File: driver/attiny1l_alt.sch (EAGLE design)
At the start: 6 parts, among them IC1 ATTiny85, IC3 74AHC1G00DCK, IC4 LB1973M, J1 AVR_SPI_PRG_6NS

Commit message: correct net name
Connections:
- net N$6 renamed RESET-
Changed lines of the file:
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@@
 </segment>
 </net>
-<net name="N$6" class="0">
+<net name="RESET-" class="0">
 <segment>
 <pinref part="IC1" gate="G$1" pin="PB5/PCINT5/!RESET!/ADC0/DW"/>

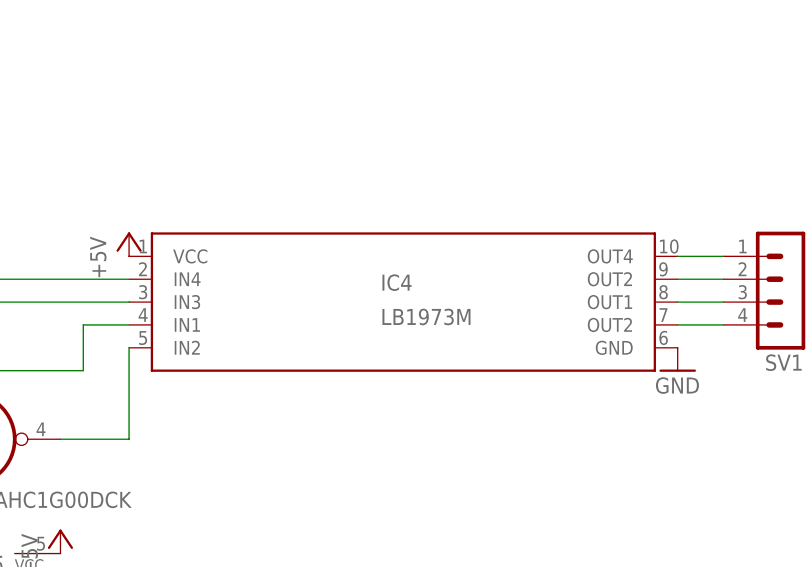
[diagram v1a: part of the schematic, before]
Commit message: the footpring was actually a bit too wide, made it 20mils narrower
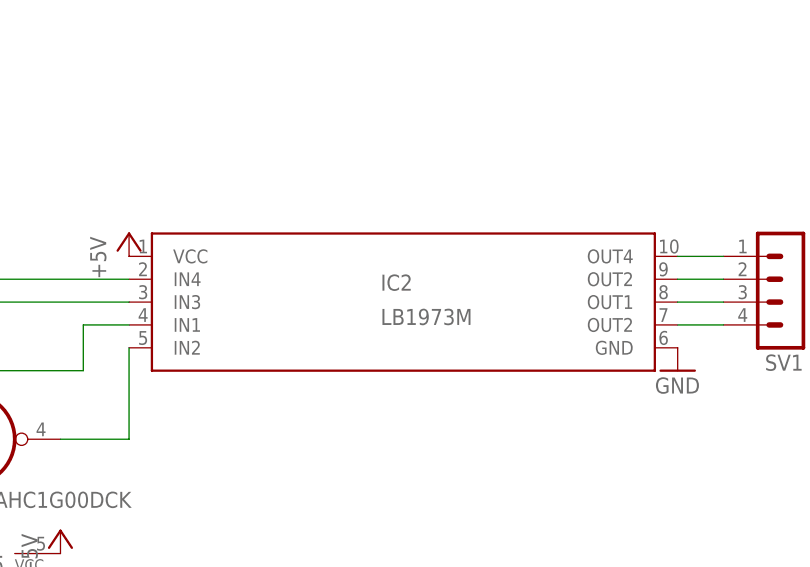
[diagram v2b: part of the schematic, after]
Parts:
- renumbered IC4 to IC2
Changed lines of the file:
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@@
 <part name="P+6" library="supply1" deviceset="+5V" device=""/>
 <part name="GND6" library="supply1" deviceset="GND" device=""/>
-<part name="IC4" library="LB1973M" deviceset="LB1973M" device=""/>
+<part name="IC2" library="LB1973M" deviceset="LB1973M" device=""/>
 </parts>
 <sheets>
@@
 <instance part="P+6" gate="1" x="40.64" y="55.88"/>
 <instance part="GND6" gate="1" x="33.02" y="55.88" rot="R180"/>
-<instance part="IC4" gate="G$1" x="149.86" y="78.74"/>
+<instance part="IC2" gate="G$1" x="149.86" y="78.74"/>
 </instances>
 <busses>
@@
 <wire x1="111.76" y1="63.5" x2="119.38" y2="63.5" width="0.1524" layer="91"/>
 <wire x1="119.38" y1="63.5" x2="119.38" y2="73.66" width="0.1524" layer="91"/>
-<pinref part="IC4" gate="G$1" pin="IN2"/>
+<pinref part="IC2" gate="G$1" pin="IN2"/>
 </segment>
 </net>
 <net name="IN4" class="0">
 <segment>
-<pinref part="IC4" gate="G$1" pin="IN4"/>
 <pinref part="IC1" gate="G$1" pin="PB4/PCINT4/ADC2"/>
 <wire x1="50.8" y1="78.74" x2="96.52" y2="78.74" width="0.1524" layer="91"/>
 <wire x1="96.52" y1="78.74" x2="96.52" y2="81.28" width="0.1524" layer="91"/>
 <wire x1="96.52" y1="81.28" x2="119.38" y2="81.28" width="0.1524" layer="91"/>
+<pinref part="IC2" gate="G$1" pin="IN4"/>
 </segment>
 </net>
@@
 <wire x1="53.34" y1="109.22" x2="53.34" y2="71.12" width="0.1524" layer="91"/>
 <junction x="53.34" y="71.12"/>
-<pinref part="IC4" gate="G$1" pin="IN1"/>
+<pinref part="IC2" gate="G$1" pin="IN1"/>
 </segment>
 </net>
 <net name="IN3" class="0">
 <segment>
-<pinref part="IC4" gate="G$1" pin="IN3"/>
 <pinref part="IC1" gate="G$1" pin="PB3/PCINT3/CLKI/ADC3"/>
 <wire x1="50.8" y1="76.2" x2="99.06" y2="76.2" width="0.1524" layer="91"/>
 <wire x1="99.06" y1="76.2" x2="99.06" y2="78.74" width="0.1524" layer="91"/>
 <wire x1="99.06" y1="78.74" x2="119.38" y2="78.74" width="0.1524" layer="91"/>
+<pinref part="IC2" gate="G$1" pin="IN3"/>
 </segment>
 </net>
@@
 <segment>
 <pinref part="GND4" gate="1" pin="GND"/>
-<pinref part="IC4" gate="G$1" pin="GND"/>
+<pinref part="IC2" gate="G$1" pin="GND"/>
 </segment>
 </net>
@@
 <segment>
 <pinref part="P+1" gate="1" pin="+5V"/>
-<pinref part="IC4" gate="G$1" pin="VCC"/>
+<pinref part="IC2" gate="G$1" pin="VCC"/>
 </segment>
 </net>
@@
 <pinref part="SV1" gate="1" pin="1"/>
 <wire x1="185.42" y1="83.82" x2="180.34" y2="83.82" width="0.1524" layer="91"/>
-<pinref part="IC4" gate="G$1" pin="OUT4"/>
+<pinref part="IC2" gate="G$1" pin="OUT4"/>
 </segment>
 </net>
@@
 <pinref part="SV1" gate="1" pin="2"/>
 <wire x1="185.42" y1="81.28" x2="180.34" y2="81.28" width="0.1524" layer="91"/>
-<pinref part="IC4" gate="G$1" pin="OUT2@1"/>
+<pinref part="IC2" gate="G$1" pin="OUT2@1"/>
 </segment>
 </net>
@@
 <pinref part="SV1" gate="1" pin="3"/>
 <wire x1="185.42" y1="78.74" x2="180.34" y2="78.74" width="0.1524" layer="91"/>
-<pinref part="IC4" gate="G$1" pin="OUT1"/>
+<pinref part="IC2" gate="G$1" pin="OUT1"/>
 </segment>
 </net>
@@
 <pinref part="SV1" gate="1" pin="4"/>
 <wire x1="185.42" y1="76.2" x2="180.34" y2="76.2" width="0.1524" layer="91"/>
-<pinref part="IC4" gate="G$1" pin="OUT2"/>
+<pinref part="IC2" gate="G$1" pin="OUT2"/>
 </segment>
 </net>

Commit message: added bypass caps, hopefully it helps with the weird clock/reset issues we are having
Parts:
- added C1, C2: (no value), rcl:C-EUC0805
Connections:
- net +5V: now also C1.2, C2.1
- net GND: now also C1.1, C2.2
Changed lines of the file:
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@@
 <part name="GND6" library="supply1" deviceset="GND" device=""/>
 <part name="IC2" library="LB1973M" deviceset="LB1973M" device=""/>
+<part name="C1" library="rcl" deviceset="C-EU" device="C0805"/>
+<part name="C2" library="rcl" deviceset="C-EU" device="C0805"/>
 </parts>
 <sheets>
@@
 <instance part="GND6" gate="1" x="33.02" y="55.88" rot="R180"/>
 <instance part="IC2" gate="G$1" x="149.86" y="78.74"/>
+<instance part="C1" gate="G$1" x="104.14" y="40.64" rot="R90"/>
+<instance part="C2" gate="G$1" x="53.34" y="66.04" rot="R90"/>
 </instances>
 <busses>
@@
 <pinref part="IC3" gate="P" pin="GND"/>
 <pinref part="GND1" gate="1" pin="GND"/>
+<pinref part="C1" gate="G$1" pin="1"/>
+<wire x1="101.6" y1="40.64" x2="91.44" y2="40.64" width="0.1524" layer="91"/>
+<wire x1="91.44" y1="40.64" x2="91.44" y2="50.8" width="0.1524" layer="91"/>
+<wire x1="91.44" y1="50.8" x2="96.52" y2="50.8" width="0.1524" layer="91"/>
+<junction x="96.52" y="50.8"/>
 </segment>
 <segment>
 <pinref part="IC1" gate="G$1" pin="GND"/>
 <pinref part="GND3" gate="1" pin="GND"/>
+<wire x1="50.8" y1="83.82" x2="63.5" y2="83.82" width="0.1524" layer="91"/>
+<wire x1="63.5" y1="83.82" x2="63.5" y2="66.04" width="0.1524" layer="91"/>
+<pinref part="C2" gate="G$1" pin="2"/>
+<wire x1="63.5" y1="66.04" x2="58.42" y2="66.04" width="0.1524" layer="91"/>
+<junction x="50.8" y="83.82"/>
+<junction x="58.42" y="66.04"/>
 </segment>
 <segment>
@@
 <pinref part="IC3" gate="P" pin="VCC"/>
 <pinref part="P+3" gate="1" pin="+5V"/>
+<pinref part="C1" gate="G$1" pin="2"/>
+<wire x1="109.22" y1="40.64" x2="111.76" y2="40.64" width="0.1524" layer="91"/>
+<wire x1="111.76" y1="40.64" x2="111.76" y2="50.8" width="0.1524" layer="91"/>
+<junction x="111.76" y="50.8"/>
 </segment>
 <segment>
 <pinref part="IC1" gate="G$1" pin="VCC"/>
 <pinref part="P+4" gate="1" pin="+5V"/>
+<pinref part="C2" gate="G$1" pin="1"/>
+<junction x="50.8" y="66.04"/>
+<pinref part="C2" gate="G$1" pin="1"/>
 </segment>
 <segment>
